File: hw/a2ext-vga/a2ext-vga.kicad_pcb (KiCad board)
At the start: 2 copper layers, 45 x 45 mm, 15 parts, among them J1 Carrier IDC20, J2 DE-15HD female

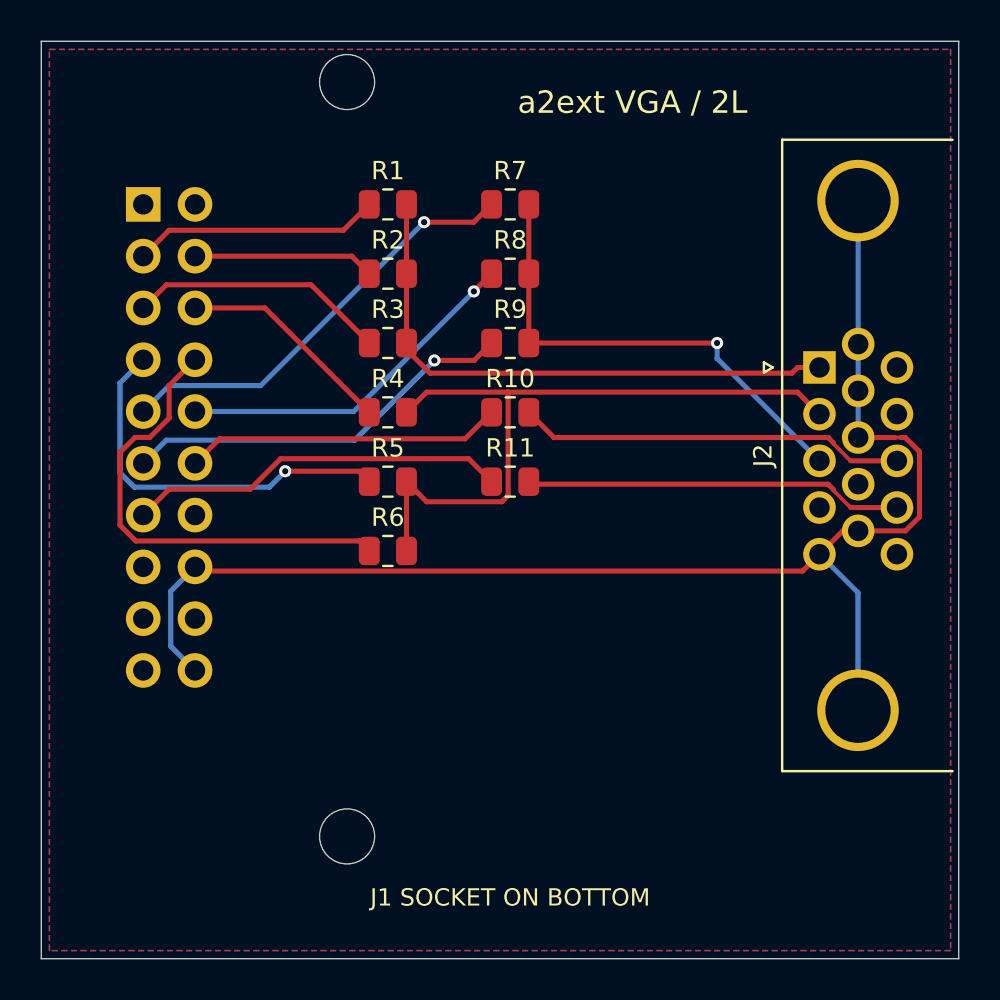
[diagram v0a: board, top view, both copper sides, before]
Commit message: Revise all prototype PCBs for through-hole assembly
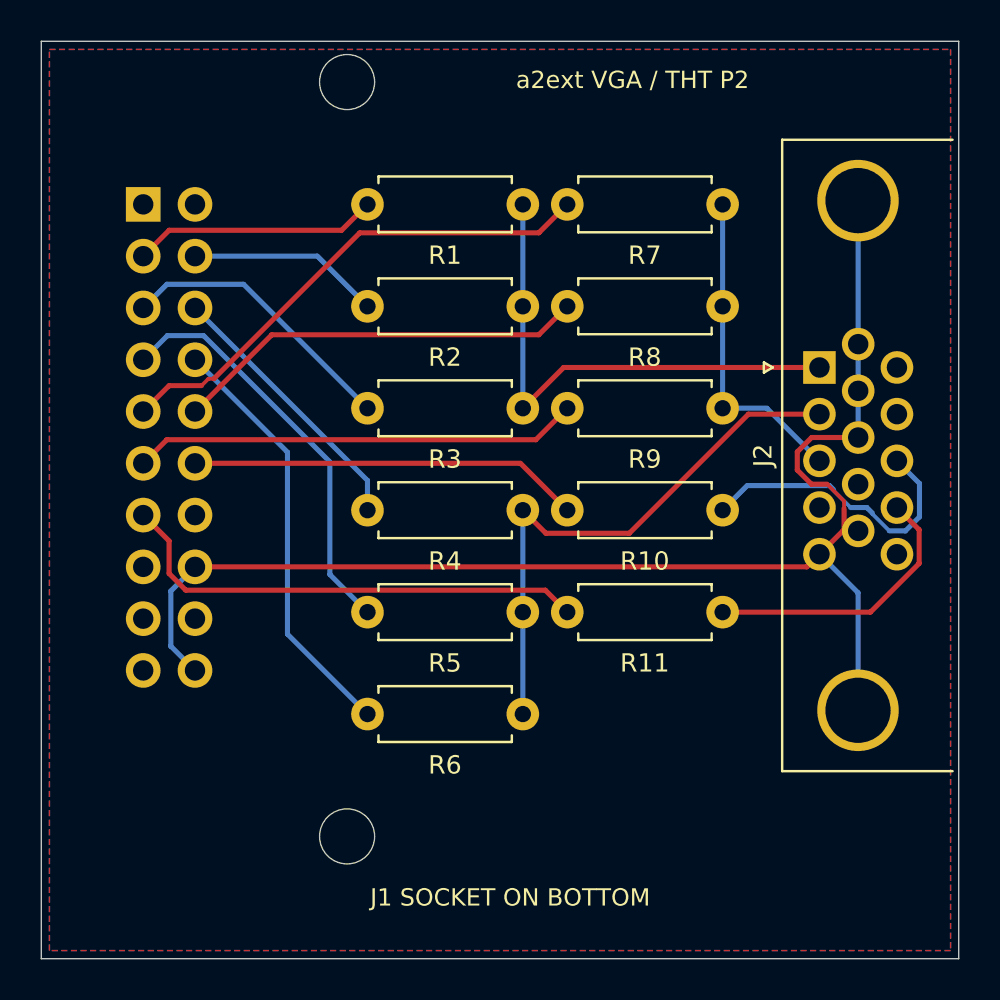
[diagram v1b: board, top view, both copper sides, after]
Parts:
- R1, R10, R11, R2, R3, R4, R5, R6, R7, R8, R9: footprint A2Ext:R0805 -> A2Ext:R_Axial_7.62
- moved R6 8.06 mm to (81.0, 98.0)
- moved R11 6.99 mm to (90.8, 93.0)
- moved R5 6.48 mm to (81.0, 93.0)
- moved R10 5.56 mm to (90.8, 88.0)
- moved R4 4.90 mm to (81.0, 88.0)
- moved R9 4.25 mm to (90.8, 83.0)
- moved R3 3.35 mm to (81.0, 83.0)
- moved R8 3.22 mm to (90.8, 78.0)
- moved R7 2.80 mm to (90.8, 73.0)
- moved R2 1.89 mm to (81.0, 78.0)
- moved R1 1.00 mm to (81.0, 73.0)
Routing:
- net /VGA_B: track 23.9 -> 15.8 mm, vias 1 -> 0
- net /VGA_G: track 35.1 -> 27.4 mm
- net /VSYNC: track 18.7 -> 23.7 mm
- net /VGA_VSYNC: track 18.6 -> 13.8 mm
- net /VGA_HSYNC: track 19.1 -> 14.6 mm
- net /B0: track 21.3 -> 25.0 mm, vias 1 -> 0
- net /HSYNC: track 15.6 -> 19.2 mm
- net /B1: track 17.3 -> 20.4 mm, vias 1 -> 0
- net /G0: track 10.7 -> 13.4 mm
- net /VGA_R: track 28.0 -> 25.4 mm
- net /B2: track 19.5 -> 21.9 mm, vias 1 -> 0
- net /G2: track 22.8 -> 20.9 mm
- net /GND: track 69.3 -> 67.9 mm
- net /G1: track 19.1 -> 20.3 mm, vias 1 -> 0
- net /R2: track 12.7 -> 14.0 mm
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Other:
- board text added: "a2ext VGA / THT P2"
- board text removed: "a2ext VGA / 2L"
